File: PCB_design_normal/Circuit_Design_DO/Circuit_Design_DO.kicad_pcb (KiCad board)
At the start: 4 copper layers, 120 x 80 mm, 121 parts, among them J1 Power, J10 ICSP, J3 Analog, J4 PWM, J5 Analog, J6 COMUNICATION, J7 Digital, J8 Conn_Coaxial, J9 USB_C_Receptacle_USB2.0_16P, K1 SANYOU_SRD_Form_A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

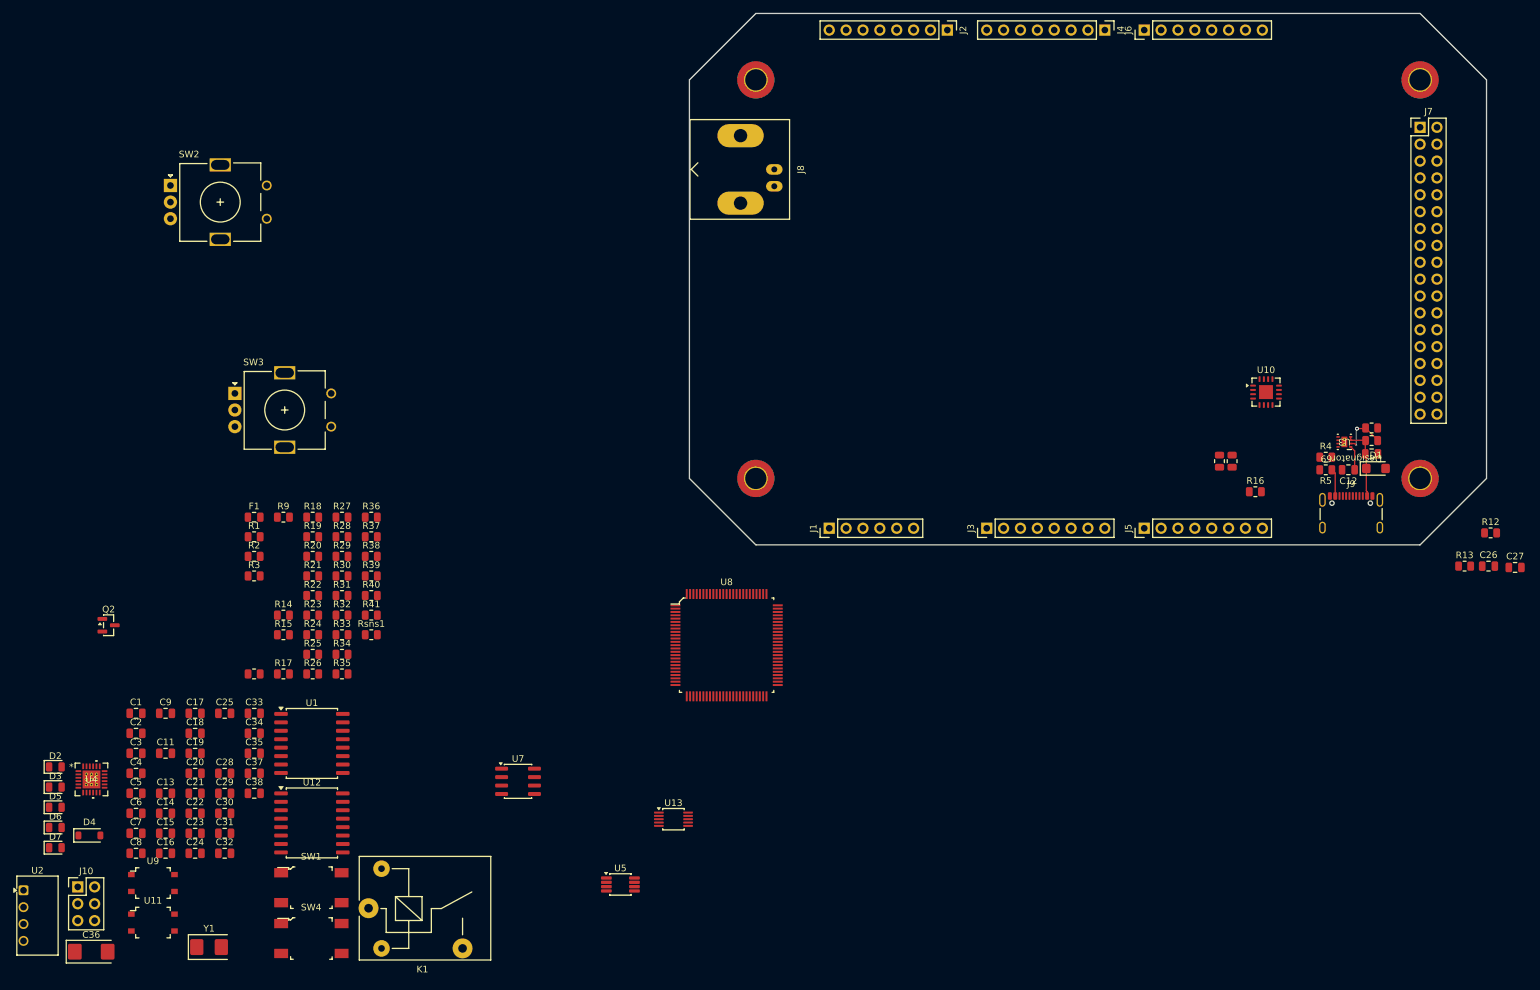
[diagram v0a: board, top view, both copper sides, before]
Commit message: Power circuits and microcontroller+oscillator placement
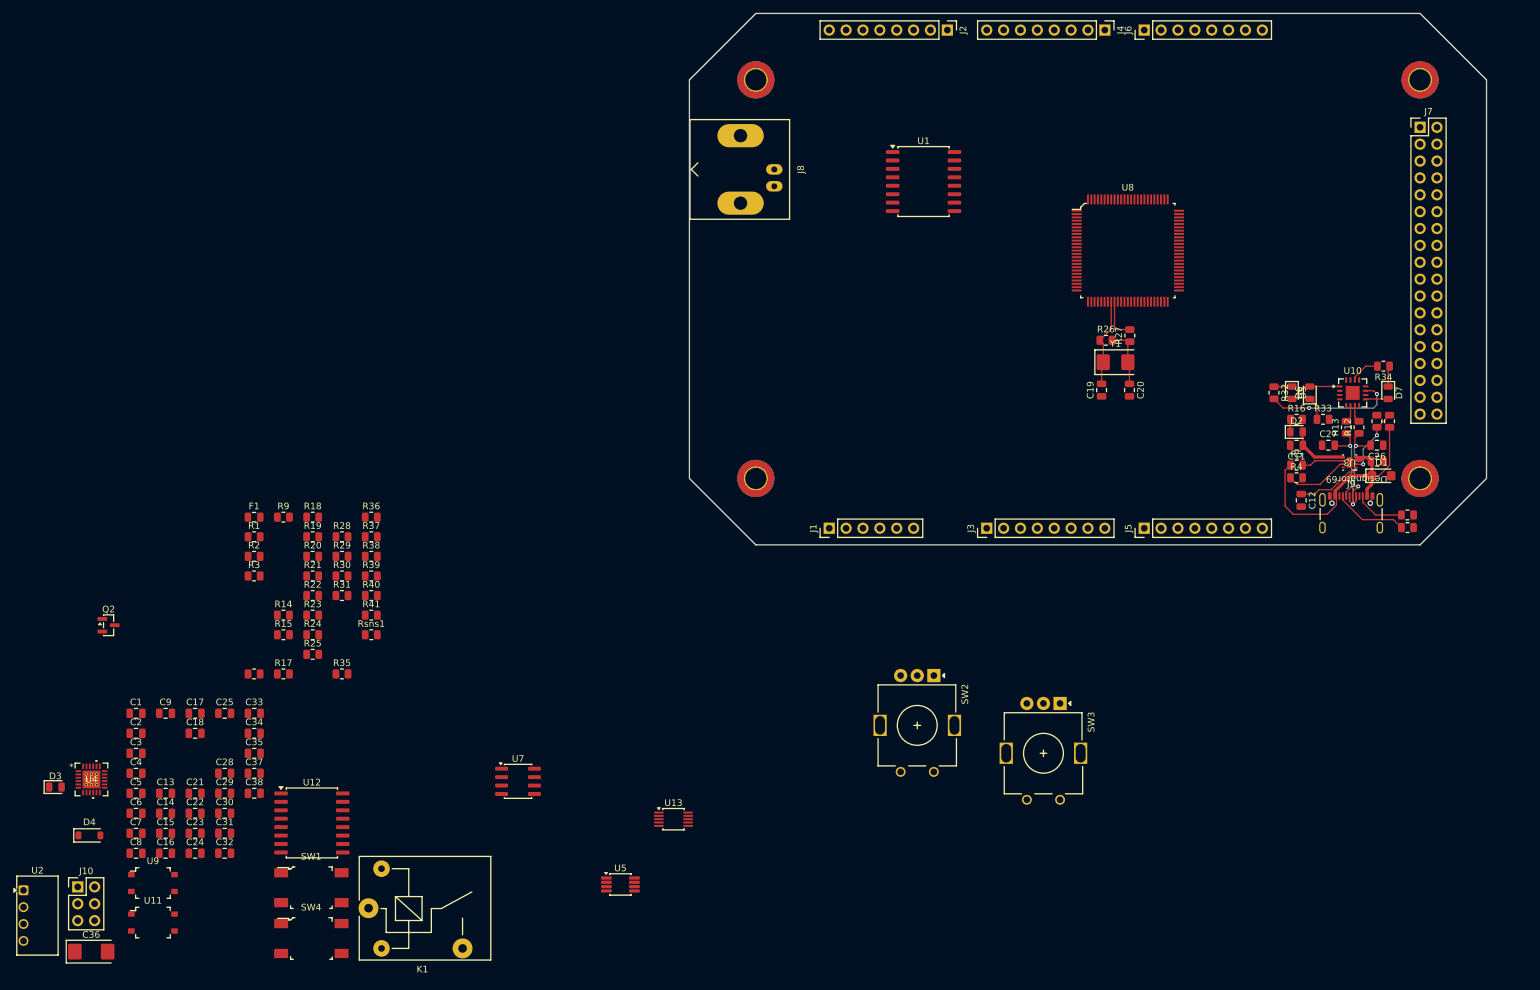
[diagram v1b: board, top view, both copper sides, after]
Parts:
- moved D7 212.0 mm to (225.2, 87.1), turned to -90 degrees
- moved D6 199.9 mm to (213.4, 87.1), turned to 90 degrees
- moved D5 196.3 mm to (210.7, 87.1), turned to -90 degrees
- moved D2 193.5 mm to (211.4, 93.0)
- moved C11 176.5 mm to (211.4, 95.0), turned to 180 degrees
- moved R34 162.7 mm to (224.5, 83.1), turned to 180 degrees
- moved Y1 162.4 mm to (184.2, 82.5)
- moved C20 152.0 mm to (186.2, 86.7), turned to -90 degrees
- moved R33 151.2 mm to (215.4, 91.1)
- moved C19 147.0 mm to (182.1, 86.7), turned to 90 degrees
- moved R32 144.2 mm to (208.0, 87.1), turned to -90 degrees
- moved SW2 136.6 mm to (156.8, 129.7), turned to -90 degrees
- moved SW3 132.7 mm to (175.8, 133.9), turned to -90 degrees
- moved R26 129.5 mm to (182.7, 79.2)
- moved U1 125.0 mm to (155.2, 55.3)
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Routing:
- net Net-(D1-A1): track 15.7 -> 42.5 mm
- net Net-(U10-CBUS1): track 0.00 -> 19.8 mm, vias 0 -> 2
- net Data-: track 0.00 -> 16.6 mm, vias 0 -> 2
- net Data+: track 0.00 -> 16.5 mm, vias 0 -> 2
- net Net-(U8A-XTAL2): track 0.00 -> 13.4 mm
- net VCCIO: track 0.00 -> 11.4 mm
- net Net-(J9-CC1): track 0.00 -> 11.1 mm
- net Net-(U3-ILM): track 0.00 -> 9.64 mm
- net Net-(C20-Pad1): track 0.00 -> 9.34 mm
- net +5VD: track 0.00 -> 8.84 mm
- net Net-(J9-CC2): track 0.00 -> 7.54 mm
- net Net-(U3-DV_DT): track 3.70 -> 10.1 mm
- net FLT_eFuse: track 0.00 -> 6.41 mm
- net Net-(U8A-XTAL1): track 0.00 -> 6.38 mm
- net Net-(U10-CBUS3): track 0.00 -> 4.51 mm
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
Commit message: Added frontend circuits, powerplanes, changed relay component
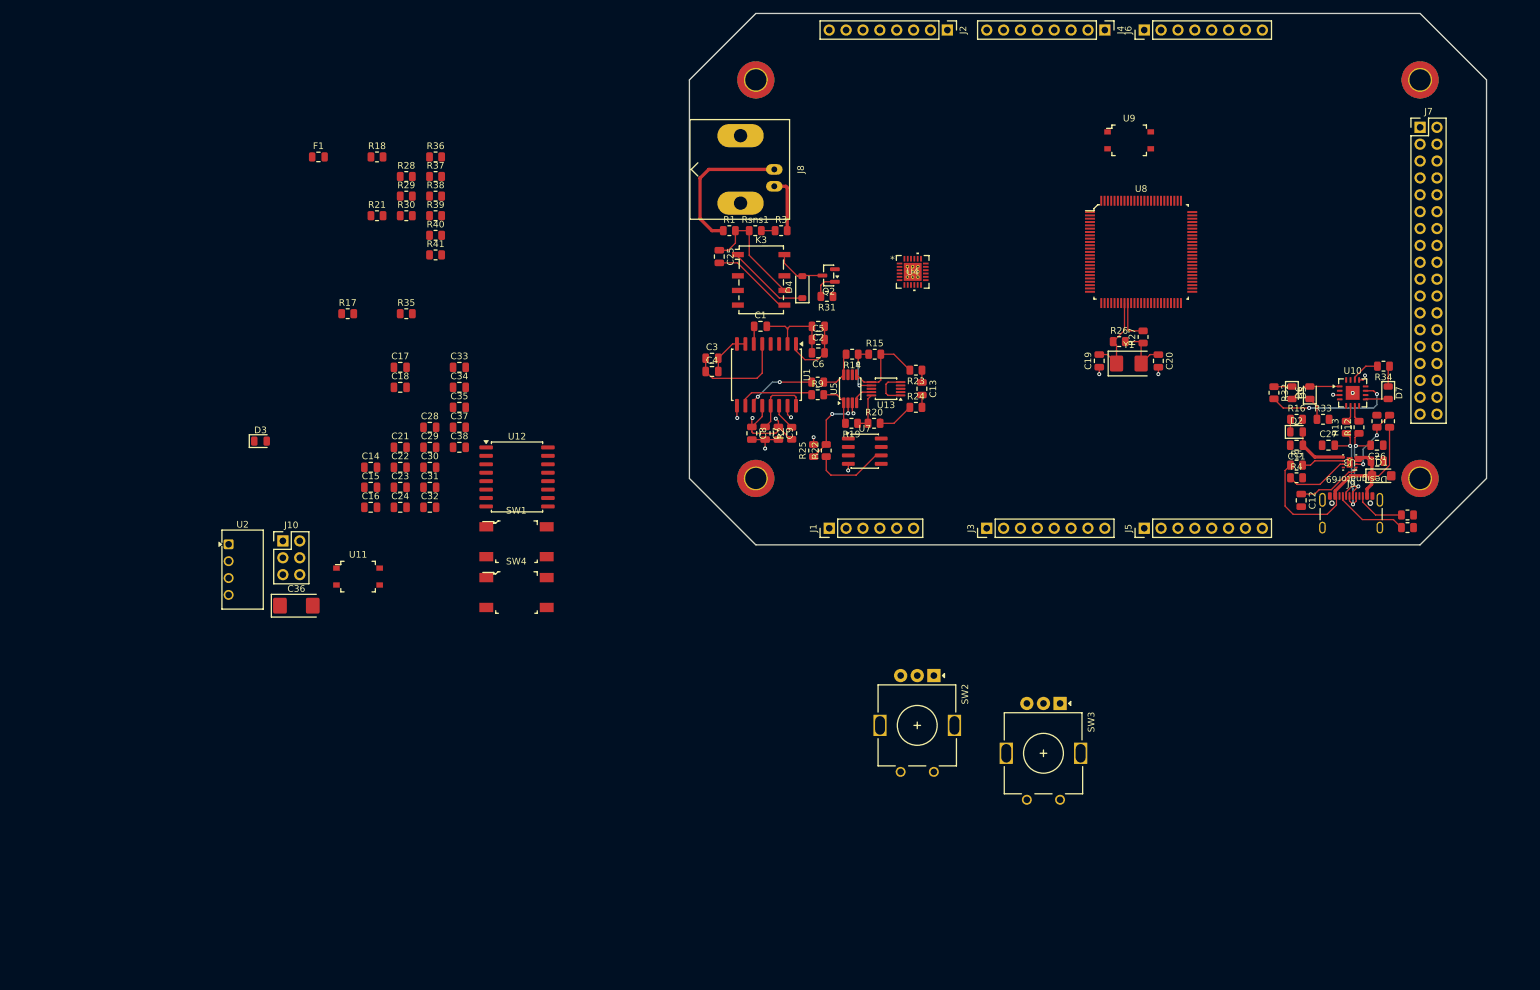
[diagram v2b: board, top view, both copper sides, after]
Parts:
- removed K1: SANYOU_SRD_Form_A, Relay_THT:Relay_SPST_SANYOU_SRD_Series_Form_A
- added K3: G6K-2, Relay_SMD:Relay_DPDT_Omron_G6K-2F-Y, F.Cu at (130.8, 70.1)
- moved U9 184.7 mm to (186.2, 49.1)
- moved U4 145.3 mm to (153.6, 68.9)
- moved D4 135.4 mm to (137.0, 71.2), turned to 90 degrees
- moved C13 129.1 mm to (155.0, 86.5), turned to -90 degrees
- moved C6 123.9 mm to (139.4, 81.1), turned to 180 degrees
- moved C5 123.3 mm to (139.4, 79.1)
- moved Q2 120.5 mm to (141.0, 69.5), turned to 180 degrees
- moved C2 119.6 mm to (139.4, 77.1), turned to 180 degrees
- moved C7 112.2 mm to (131.4, 93.2), turned to -90 degrees
- moved C8 112.2 mm to (129.4, 93.2), turned to -90 degrees
- moved C1 110.6 mm to (130.7, 77.1)
- moved C4 105.7 mm to (123.4, 83.9)
- moved C3 105.1 mm to (123.4, 81.9)
- moved C9 101.4 mm to (133.4, 93.2), turned to -90 degrees
- moved C25 101.4 mm to (124.5, 66.6), turned to -90 degrees
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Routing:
- net +5VA: track 0.00 -> 29.2 mm, vias 0 -> 3
- net Net-(U1-DCDC_HGND): track 0.00 -> 22.6 mm
- net Net-(J8-In): track 0.00 -> 22.1 mm
- net Rel_In: track 0.00 -> 18.0 mm
- net Net-(U1-HLDO_OUT): track 0.00 -> 15.7 mm
- net Rel_out: track 0.00 -> 15.1 mm
- net Net-(R15-Pad2): track 0.00 -> 13.8 mm
- net RefOut: track 0.00 -> 11.9 mm
- net Vocm: track 0.00 -> 11.7 mm, vias 0 -> 2
- net OUTN: track 0.00 -> 11.5 mm
- net AGND: track 0.00 -> 11.3 mm, vias 0 -> 5
- net OUTP: track 0.00 -> 10.6 mm, vias 0 -> 2
- net Net-(U1-DCDC_OUT): track 0.00 -> 10.3 mm
- net Net-(U1-DCDC_IN): track 0.00 -> 10.2 mm
- net Net-(R20-Pad2): track 0.00 -> 9.51 mm
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- added copper zone on In2.Cu, net +5VA
- added copper zone on In2.Cu, net +5VD
- added copper zone on In1.Cu, net AGND
- added copper zone on In1.Cu, net DGND

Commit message: Almost done PCB design and final hardware checks
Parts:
- removed C38: 100n, Capacitor_SMD:C_0805_2012Metric
- added R42: 2.4k, Resistor_SMD:R_0805_2012Metric, F.Cu at (165.6, 88.4)
- added R43: 10k, Resistor_SMD:R_0805_2012Metric, F.Cu at (159.0, 88.4)
- added U6: LTV-356T, digikey-footprints:SMD-4_4.4x3.85mm_P2.54mm, F.Cu at (162.3, 84.2)
- moved C24 160.0 mm to (225.1, 45.0), turned to -90 degrees
- moved J10 148.0 mm to (198.4, 60.1)
- moved SW1 146.3 mm to (220.8, 36.7), turned to -90 degrees
- moved R28 146.0 mm to (223.1, 45.0), turned to -90 degrees
- moved SW4 143.5 mm to (212.8, 36.7), turned to -90 degrees
- moved C35 139.1 mm to (217.2, 45.0), turned to -90 degrees
- moved R41 135.1 mm to (215.2, 45.0), turned to -90 degrees
- moved C31 133.4 mm to (205.6, 53.9), turned to 90 degrees
- moved C28 132.8 mm to (213.4, 83.0), turned to -90 degrees
- moved C32 132.0 mm to (205.6, 60.9), turned to -90 degrees
- moved R36 127.9 mm to (207.6, 74.6), turned to -90 degrees
- moved R40 126.2 mm to (207.6, 53.9), turned to 90 degrees
- moved R39 126.0 mm to (207.6, 67.6), turned to 90 degrees
- moved R38 125.9 mm to (207.6, 60.9), turned to -90 degrees
- moved C34 121.7 mm to (205.6, 67.6), turned to 90 degrees
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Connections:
- J2 pad 5: /PB6 -> 10X
- J7 pad 4: 10X -> /PA1
- R35 pad 2: rst_dn -> Net-(R35-Pad2)
- U11 pad 1: rst_dn -> Net-(R35-Pad2)
- U11 pad 2: DGND -> rst_dn
- U13 pad 1: 10X -> 10Xa
- U13 pad 5: 10X -> 10Xa
- U3 pad V: (no net) -> DGND
- U4 pad 1: /CS_D -> /CS_A
- U8 pad 25: /PB6 -> 10X
- U8 pad 77: 10X -> /PA1
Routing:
- net rst_dn: track 0.00 -> 264.8 mm, vias 0 -> 6
- net RX_ft: track 0.00 -> 118.3 mm, vias 0 -> 4
- net TX_ft: track 0.00 -> 118.0 mm, vias 0 -> 2
- net /MISO_D: track 0.00 -> 95.8 mm, vias 0 -> 3
- net /MOSI_D: track 0.00 -> 94.2 mm, vias 0 -> 3
- net AC/DC: track 0.00 -> 92.0 mm, vias 0 -> 3
- net /PB1: track 0.00 -> 88.7 mm, vias 0 -> 1
- net 10X: track 6.05 -> 89.7 mm, vias 0 -> 2
- net /PB0: track 0.00 -> 83.4 mm, vias 0 -> 1
- net Relay_ACDC: track 0.00 -> 78.7 mm, vias 0 -> 4
- net /PD3: track 0.00 -> 76.0 mm
- net +5VD: track 8.84 -> 84.6 mm, vias 0 -> 17
- net Net-(U8A-PK7(ADC15/PCINT23)): track 0.00 -> 74.1 mm, vias 0 -> 1
- net DGND: track 4.97 -> 78.1 mm, vias 5 -> 45
- net /PD2: track 0.00 -> 71.1 mm
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
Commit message: Finished PCB and electronic design
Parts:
- added 5Va: TestPoint_Pad_1.0x1.0mm, TestPoint:TestPoint_Pad_1.0x1.0mm, F.Cu at (158.7, 92.8)
- added AGND: TestPoint_Pad_1.0x1.0mm, TestPoint:TestPoint_Pad_1.0x1.0mm, F.Cu at (161.2, 92.8)
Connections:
- U4 pad V: (no net) -> AGND
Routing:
- net /PG2: track 0.00 -> 55.5 mm, vias 0 -> 3
- net /PC6: track 0.00 -> 48.4 mm, vias 0 -> 2
- net /PC4: track 0.00 -> 48.0 mm, vias 0 -> 2
- net /PC5: track 0.00 -> 45.8 mm, vias 0 -> 2
- net /PC7: track 0.00 -> 43.1 mm, vias 0 -> 2
- net /PC3: track 0.00 -> 43.1 mm, vias 0 -> 2
- net /PC2: track 7.98 -> 45.5 mm, vias 1 -> 2
- net Net-(U1-DCDC_HGND): track 39.2 -> 46.8 mm
- net /MISO_D: track 95.8 -> 101.2 mm
- net /PB0: track 83.4 -> 88.4 mm
- net /MOSI_D: track 94.2 -> 99.0 mm
- net AGND: track 34.6 -> 38.5 mm
- net +5VA: track 56.5 -> 60.4 mm
- net /PB1: track 88.7 -> 91.8 mm
- net 10X: track 89.7 -> 90.9 mm
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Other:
- board text added: "+5V"
- board text added: "0"
- board text added: "1"
- board text added: "10"
- board text added: "11"
- board text added: "12"
- board text added: "13"
- board text added: "14"
- board text added: "15"
- board text added: "16"
- board text added: "17"
- board text added: "18"
- board text added: "19"
- board text added: "2"
- board text added: "20"
- board text added: "21"
- board text added: "22"
- board text added: "23"
- board text added: "24"
- board text added: "25"
- board text added: "26"
- board text added: "27"
- board text added: "28"
- board text added: "29"
- board text added: "3"
- board text added: "30"
- board text added: "31"
- board text added: "33"
- board text added: "34"
- board text added: "35"
- board text added: "36"
- board text added: "37"
- board text added: "38"
- board text added: "39"
- board text added: "4"
- board text added: "40"
- board text added: "41"
- board text added: "42"
- board text added: "43"
- board text added: "44"
- board text added: "45"
- board text added: "46"
- board text added: "47"
- board text added: "48"
- board text added: "49"
- board text added: "5"
- board text added: "50"
- board text added: "51"
- board text added: "52"
- board text added: "53"
- board text added: "5V"
- board text added: "6"
- board text added: "7"
- board text added: "8"
- board text added: "9"
- board text added: "A1"
- board text added: "A10"
- board text added: "A11"
- board text added: "A12"
- board text added: "A13"
- board text added: "A14"
- board text added: "A15"
- board text added: "A2"
- board text added: "A3"
- board text added: "A4"
- board text added: "A5"
- board text added: "A6"
- board text added: "A7"
- board text added: "A8"
- board text added: "A9"
- board text added: "AC/DC"
- board text added: "AREF"
- board text added: "Analog"
- board text added: "Digital"
- board text added: "GND"
- board text added: "Galvanically Isolated Digital Oscilloscope Rev 0.0"
- board text added: "ICSP"
- board text added: "JLCJLCJLCJLC"
- board text added: "RESET"

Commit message: Final touches
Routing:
- net DGND: vias 46 -> 55
- net AGND: vias 19 -> 20
- added copper zone on B.Cu, net AGND
- added copper zone on F.Cu, net AGND
- added copper zone on B.Cu, net DGND
- added copper zone on F.Cu, net DGND
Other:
- board text added: "Builtin LED"
- board text added: "Power"
- board text added: "RX"
- board text added: "SUSP"
- board text added: "TX"

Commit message: added Doc template
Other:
- board text added: "Designed by Furtună Cristian IESC UNITBV"
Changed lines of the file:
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@@
+		)
+	)
+	(gr_text "Designed by \nFurtună Cristian\nIESC UNITBV"
+		(at 131.3 33.5 0)
+		(layer "F.SilkS")
+		(effects
+			(font
+				(size 0.5 0.5)
+				(thickness 0.0625)
+			)
+			(justify left bottom)
 		)
 	)
